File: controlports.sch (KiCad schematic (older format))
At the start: 4 parts, among them CN3 Port1 Male DB9, CN4 Port2 Male DB9, U2 4066

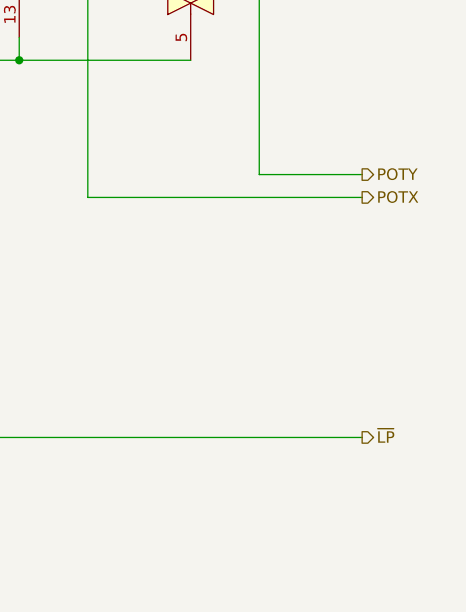
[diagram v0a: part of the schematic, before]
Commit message: Clean up schematic
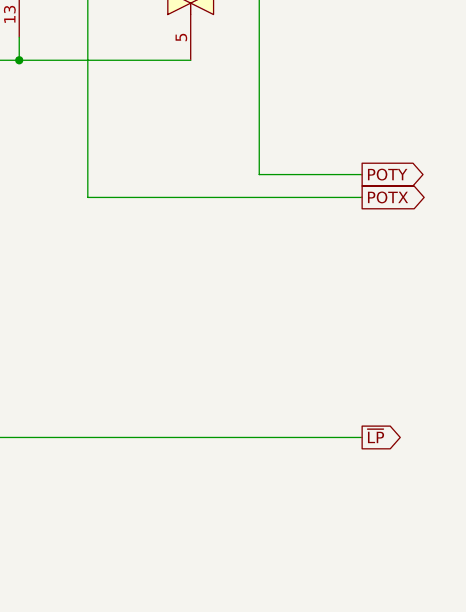
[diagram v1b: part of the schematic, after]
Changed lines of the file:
@@
 Wire Wire Line
 	6650 3200 7100 3200
-Text HLabel 7100 3200 2    50   Output ~ 0
-POTY
-Text HLabel 7100 3300 2    50   Output ~ 0
-POTX
 Text Label 4850 2700 0    50   ~ 0
 COL7
@@
 Text Label 4400 4350 0    50   ~ 0
 ROW4
-Text HLabel 7100 4350 2    50   Output ~ 0
-~LP
 Wire Wire Line
 	5900 1450 5900 2300
@@
 Wire Bus Line
 	4300 2900 4300 4800
+Text GLabel 7100 3200 2    50   Output ~ 0
+POTY
+Text GLabel 7100 3300 2    50   Output ~ 0
+POTX
+Text GLabel 7100 4350 2    50   Output ~ 0
+~LP
 $EndSCHEMATC
